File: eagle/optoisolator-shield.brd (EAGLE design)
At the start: 101.6 x 53.3 mm, 51 parts, among them Q1 NPN, Q2 NPN, Q3 NPN, Q4 NPN, Q5 NPN, Q6 NPN, U1 OPTO, U2 OPTO, U3 OPTO

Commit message: fixed XIO orientation error propagated from HackEEG shield
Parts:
- moved U$5 4.46 mm to (1.78, 5.89)
- moved U$2 0.05 mm to (1.78, 51.9)
- turned JP4 to 270 degrees
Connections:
- removed net N$602: JP4.35, JP4.36
- net GND: now also JP4.35, JP4.36
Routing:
- net D41: track 99.1 -> 126.9 mm, vias 3 -> 2
- net D43: track 84.5 -> 105.5 mm, vias 1 -> 0
- net D42: track 89.7 -> 105.8 mm
- net D40: track 91.5 -> 84.1 mm
- net D38: track 104.9 -> 98.5 mm
- net D45: track 90.8 -> 94.6 mm
- net D39: track 92.3 -> 96.0 mm
- net D44: track 94.9 -> 91.8 mm
- net N$602: track 2.54 -> 0.00 mm
- net OPTO_OUT_1B: track 76.1 -> 77.3 mm
- removed copper zone on layer 1, net D43
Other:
- board text added: "0"
- board text added: "1"
- board text added: "10"
- board text added: "11"
- board text added: "12"
- board text added: "13"
- board text added: "14"
- board text added: "15"
- board text added: "16"
- board text added: "17"
- board text added: "18"
- board text added: "19"
- board text added: "2"
- board text added: "20"
- board text added: "21"
- board text added: "22"
- board text added: "23"
- board text added: "24"
- board text added: "25"
- board text added: "26"
- board text added: "27"
- board text added: "28"
- board text added: "29"
- board text added: "3"
- board text added: "30"
- board text added: "31"
- board text added: "32"
- board text added: "33"
- board text added: "34"
- board text added: "35"
- board text added: "36"
- board text added: "37"
- board text added: "38"
- board text added: "3V3"
- board text added: "4"
- board text added: "46"
- board text added: "47"
- board text added: "48"
- board text added: "49"
- board text added: "5"
- board text added: "50"
- board text added: "51"
- board text added: "52"
- board text added: "53"
- board text added: "5V"
- board text added: "6"
- board text added: "7"
- board text added: "8"
- board text added: "9"
- board text added: "A0"
- board text added: "A1"
- board text added: "A10"
- board text added: "A11"
- board text added: "A12"
- board text added: "A13"
- board text added: "A14"
- board text added: "A15"
- board text added: "A2"
- board text added: "A3"
- board text added: "A4"
- board text added: "A5"
- board text added: "A6"
- board text added: "A7"
- board text added: "A8"
- board text added: "A9"
- board text added: "AREF"
- board text added: "GND"
- board text added: "IOREF"
- board text added: "RESET"
- board text added: "SCL1"
- board text added: "SDA1"
- board text added: "StarCat Optoisolator Shield"
- board text added: "VIN"
- board text added: "v1.1"
- board text removed: "StarCat Optoisolator Shield v1.0"

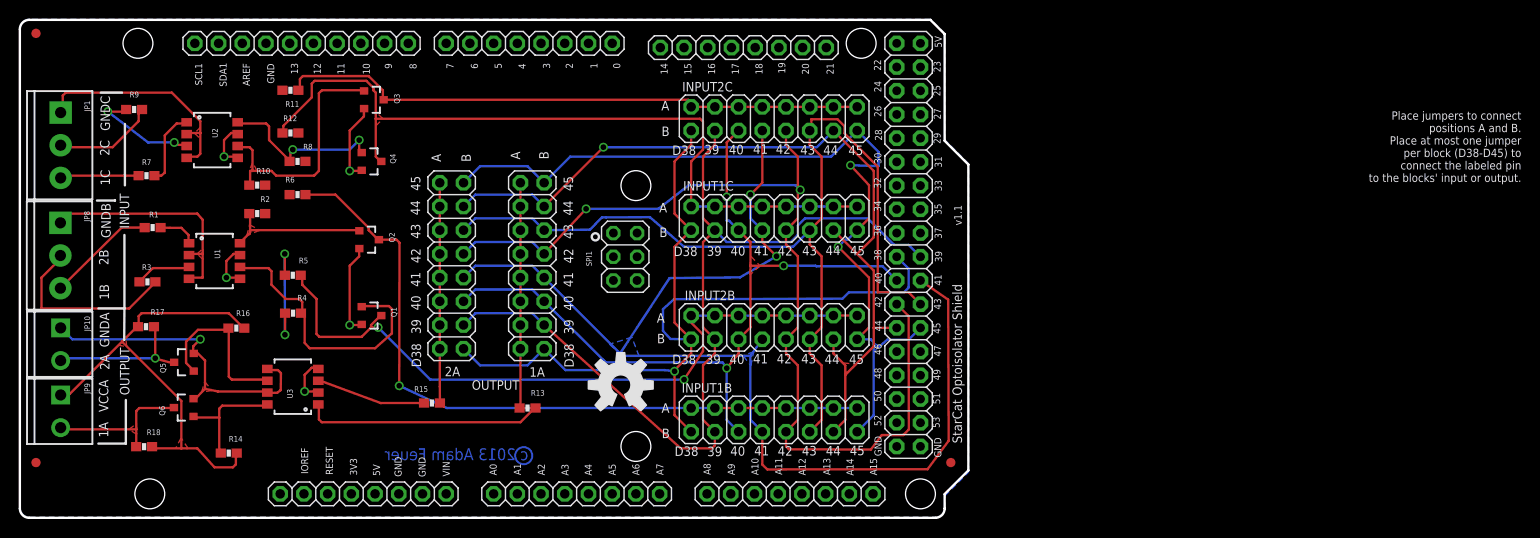
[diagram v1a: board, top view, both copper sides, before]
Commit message: updated silkscreen with correct dac0/1 and canrx/tx labels; updated fiducials so 2 share the same X and 2 share the same Y coordinates
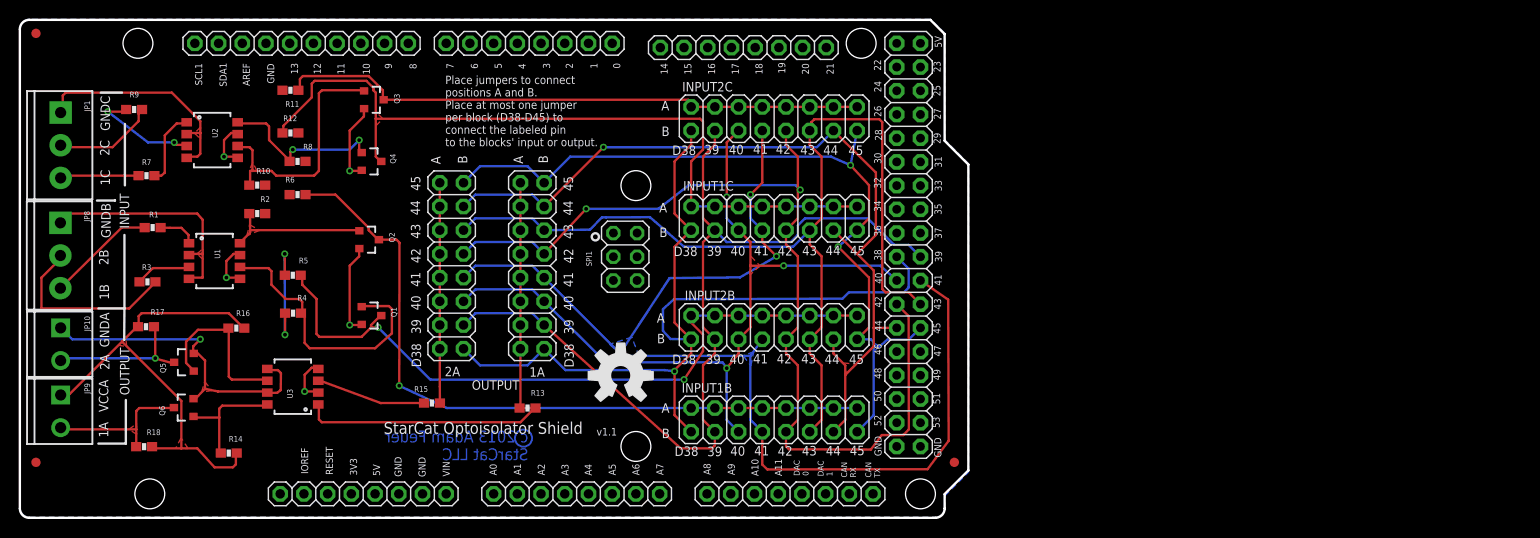
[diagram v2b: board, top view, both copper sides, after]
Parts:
- Q1, Q2, Q3, Q4, Q5, Q6: value NPN -> MMBT2222ALT3G
- moved U$1 1.02 mm to (64.4, 15.2)
- moved U$6 0.38 mm to (100.2, 5.92)
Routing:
- net D45: track 94.6 -> 88.9 mm
- net D43: track 105.5 -> 107.5 mm
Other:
- board text added: "CAN RX"
- board text added: "CAN TX"
- board text added: "DAC 0"
- board text added: "DAC 1"
- board text added: "c 2013 Adam Feuer StarCat LLC"
- board text removed: "A12"
- board text removed: "A13"
- board text removed: "A14"
- board text removed: "A15"
- board text removed: "c 2013 Adam Feuer"

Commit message: improved trace clearances; changed names of inputs from 1A... to A1... for better readability
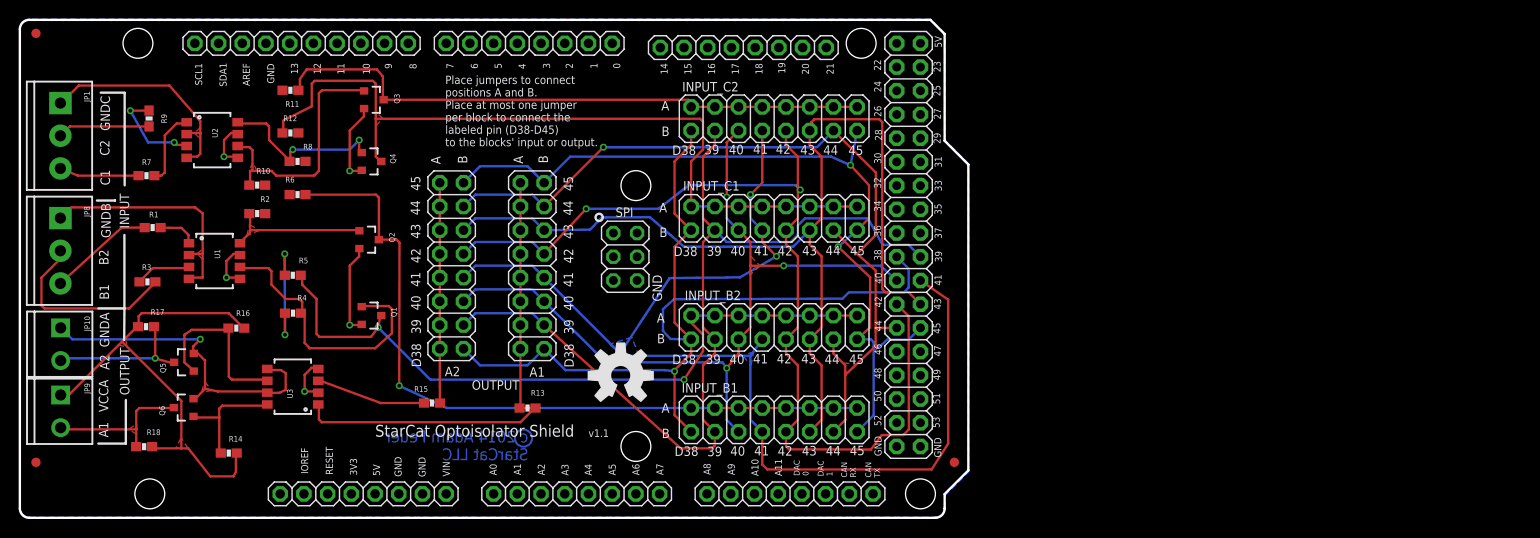
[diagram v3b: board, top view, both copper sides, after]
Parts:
- moved R9 1.87 mm to (13.9, 42.7), turned to 270 degrees
- moved JP1 1.02 mm to (4.39, 44.4)
- moved JP8 0.51 mm to (4.39, 32.1)
- renumbered 1A to A1, 2A to A2, INPUT1B to INPUT_B1, INPUT1C to INPUT_C1, INPUT2B to INPUT_B2, INPUT2C to INPUT_C2, SPI1 to SPI
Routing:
- net OPTO_OUT_1B: track 77.3 -> 79.8 mm
- net N$23: track 12.0 -> 10.2 mm
- net OPTO_OUT_2C: track 63.4 -> 65.0 mm
- net EXT_VCC: track 50.0 -> 51.5 mm
- net IN4: track 11.0 -> 9.91 mm
- net OPTO_OUT_1C: track 84.5 -> 85.5 mm
- net EXT_GND_2: track 35.5 -> 36.5 mm
- net OUT2N3: track 18.2 -> 18.8 mm
- net EXT_GND_1: track 24.7 -> 24.1 mm
- net D39: track 96.0 -> 96.5 mm
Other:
- board text added: "B1"
- board text added: "B2"
- board text added: "C1"
- board text added: "C2"
- board text added: "Place jumpers to connect positions A and B. Place at most one jumper per block to connect the labeled pin (D38-D45) to the blocks' input or output."
- board text added: "c 2014 Adam Feuer StarCat LLC"
- board text removed: "1A"
- board text removed: "1B"
- board text removed: "1C"
- board text removed: "2A"
- board text removed: "2B"
- board text removed: "2C"
- board text removed: "Place jumpers to connect positions A and B. Place at most one jumper per block (D38-D45) to connect the labeled pin to the blocks' input or output."
- board text removed: "c 2013 Adam Feuer StarCat LLC"

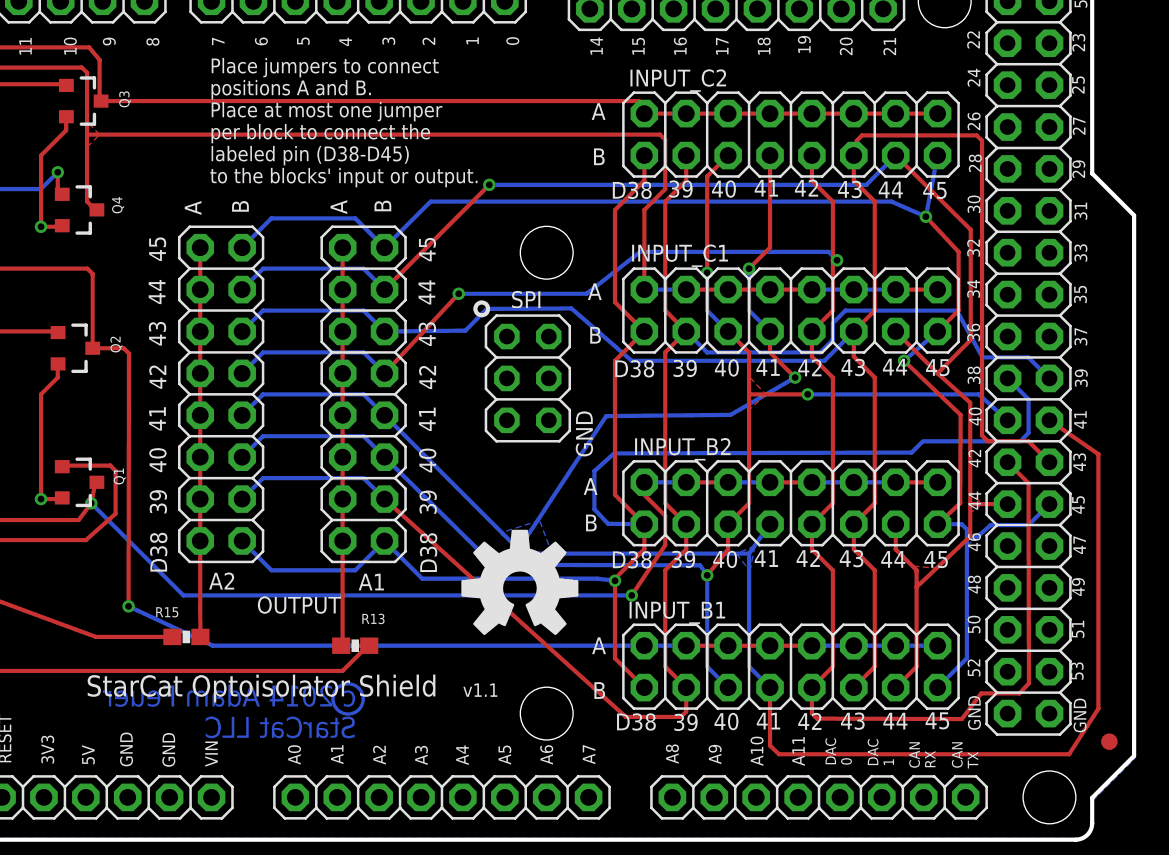
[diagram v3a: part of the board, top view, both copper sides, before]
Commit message: updated schematic renaming inputs/outputs 1A... to A1... for clarity
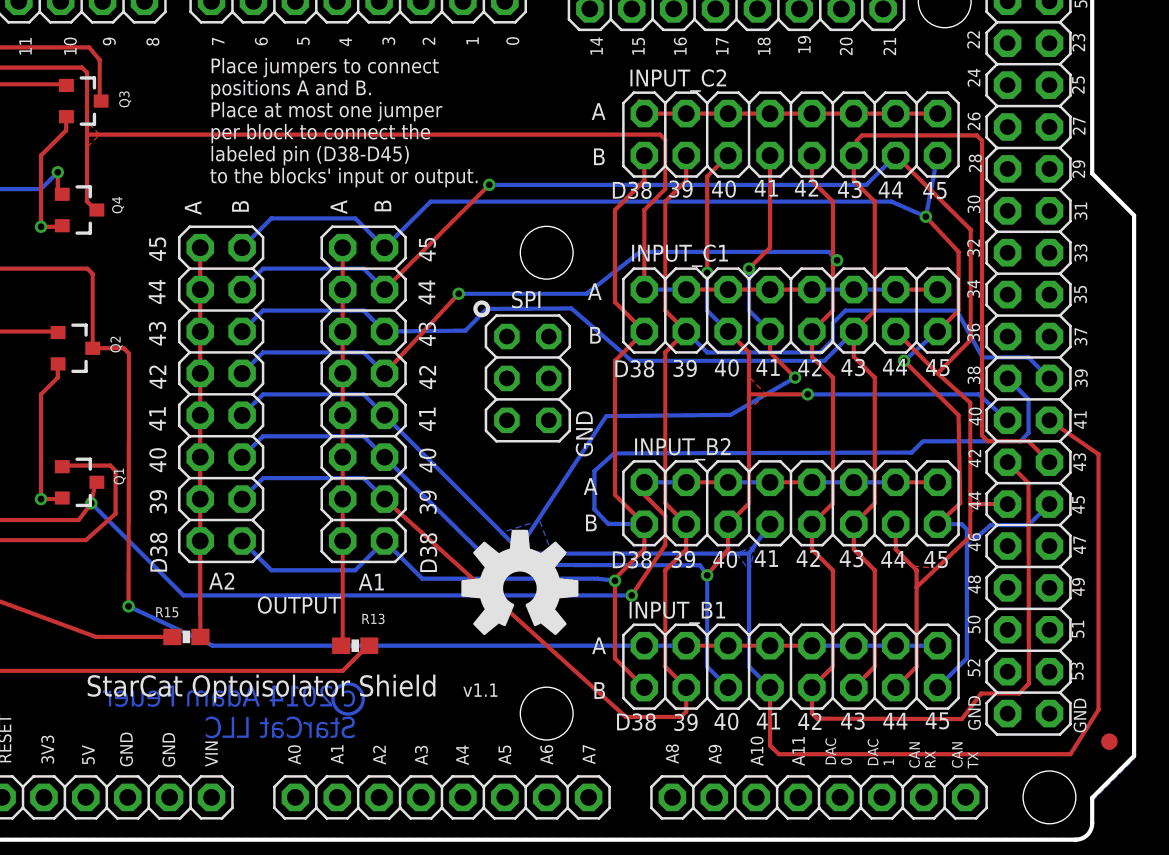
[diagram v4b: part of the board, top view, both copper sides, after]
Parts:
- U1, U2, U3: value OPTO -> ILD213T
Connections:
- net IN1 renamed IN_B1
- net IN2 renamed IN_B2
- net IN3 renamed IN_C1
- net IN4 renamed IN_C2
- net OPTO_IN_1A renamed OPTO_IN_A1
- net OPTO_IN_2A renamed OPTO_IN_A2
- net OPTO_OUT_1B renamed OPTO_OUT_B1
- net OPTO_OUT_1C renamed OPTO_OUT_C1
- net OPTO_OUT_2B renamed OPTO_OUT_B2
- net OUT5 renamed OUT_A1
- net OUT6 renamed OUT_A2
- new net OPTO_OUT_C2: Q3.3, R11.1
- net OPTO_OUT_2C: no longer Q3.3, R11.1
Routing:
- net OPTO_OUT_2C: track 65.0 -> 18.7 mm
- net OPTO_OUT_C2: track 0.00 -> 13.7 mm
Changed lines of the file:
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@@
 <element name="U$6" library="adafruit" package="FIDUCIAL_1MM" value="FIDUCIAL" x="100.1522" y="5.9182" smashed="yes"/>
 <element name="U$2" library="adafruit" package="FIDUCIAL_1MM" value="FIDUCIAL" x="1.778" y="51.8668" smashed="yes"/>
-<element name="U2" library="SparkFun" package="SO08-2" value="OPTO" x="20.6502" y="40.4368" smashed="yes" rot="R270">
+<element name="U2" library="SparkFun" package="SO08-2" value="ILD213T" x="20.6502" y="40.4368" smashed="yes" rot="R270">
 <attribute name="VALUE" x="20.0152" y="41.7068" size="0.4064" layer="27" rot="R270"/>
 <attribute name="NAME" x="20.6502" y="41.7068" size="0.6096" layer="25" font="vector" rot="R270"/>
@@
 <attribute name="VALUE" x="5.6642" y="45.6692" size="0.4064" layer="27" rot="R270"/>
 </element>
-<element name="U1" library="SparkFun" package="SO08-2" value="OPTO" x="20.9042" y="27.4828" smashed="yes" rot="R270">
+<element name="U1" library="SparkFun" package="SO08-2" value="ILD213T" x="20.9042" y="27.4828" smashed="yes" rot="R270">
 <attribute name="VALUE" x="20.2692" y="28.7528" size="0.4064" layer="27" rot="R270"/>
 <attribute name="NAME" x="20.9042" y="28.7528" size="0.6096" layer="25" font="vector" rot="R270"/>
@@
 <attribute name="VALUE" x="5.6642" y="33.3502" size="0.4064" layer="27" rot="R270"/>
 </element>
-<element name="U3" library="SparkFun" package="SO08-2" value="OPTO" x="29.2862" y="14.0208" smashed="yes" rot="R90">
+<element name="U3" library="SparkFun" package="SO08-2" value="ILD213T" x="29.2862" y="14.0208" smashed="yes" rot="R90">
 <attribute name="VALUE" x="29.9212" y="12.7508" size="0.4064" layer="27" rot="R90"/>
 <attribute name="NAME" x="29.2862" y="12.7508" size="0.6096" layer="25" font="vector" rot="R90"/>
@@
 <wire x1="28.448" y1="19.5834" x2="28.4616" y2="21.8948" width="0.254" layer="1"/>
 </signal>
-<signal name="IN2">
+<signal name="IN_B2">
 <contactref element="R3" pad="2"/>
 <contactref element="JP8" pad="2"/>
@@
 <wire x1="14.5542" y1="25.1968" x2="14.566" y2="25.2476" width="0.254" layer="1"/>
 </signal>
-<signal name="IN1">
+<signal name="IN_B1">
 <contactref element="R1" pad="1"/>
 <contactref element="JP8" pad="3"/>
@@
 <contactref element="JP4" pad="14"/>
 </signal>
-<signal name="IN3">
+<signal name="IN_C1">
 <contactref element="R7" pad="1"/>
 <contactref element="JP1" pad="3"/>
@@
 <wire x1="6.2738" y1="36.6268" x2="4.3942" y2="37.3992" width="0.254" layer="1"/>
 </signal>
-<signal name="IN4">
+<signal name="IN_C2">
 <contactref element="R9" pad="2"/>
 <contactref element="JP1" pad="2"/>
@@
 <wire x1="59.0042" y1="38.6588" x2="56.2102" y2="35.8648" width="0.254" layer="16"/>
 <wire x1="91.1098" y1="20.3708" x2="89.7382" y2="19.1008" width="0.254" layer="1"/>
-<wire x1="91.1352" y1="25.7302" x2="91.1098" y2="20.3708" width="0.254" layer="1"/>
-<wire x1="87.7062" y1="29.0068" x2="91.1352" y2="25.7302" width="0.254" layer="1"/>
+<wire x1="91.0082" y1="25.7048" x2="91.1098" y2="20.3708" width="0.254" layer="1"/>
+<wire x1="87.7062" y1="29.0068" x2="91.0082" y2="25.7048" width="0.254" layer="1"/>
 <via x="89.027" y="37.7444" extent="1-16" drill="0.4064"/>
 <via x="87.7062" y="29.0068" extent="1-16" drill="0.4064"/>
@@
 </polygon>
 <wire x1="99.4918" y1="23.3426" x2="96.52" y2="25.4" width="0.254" layer="1"/>
-<wire x1="99.4918" y1="7.9248" x2="99.4918" y2="23.3426" width="0.254" layer="1"/>
-<wire x1="97.7138" y1="5.1562" x2="99.4918" y2="7.9248" width="0.254" layer="1"/>
+<wire x1="99.4918" y1="7.8486" x2="99.4918" y2="23.3426" width="0.254" layer="1"/>
+<wire x1="97.79" y1="5.1562" x2="99.4918" y2="7.8486" width="0.254" layer="1"/>
 <wire x1="79.5782" y1="5.6769" x2="80.1243" y2="5.1562" width="0.254" layer="1"/>
-<wire x1="80.1243" y1="5.1562" x2="97.7138" y2="5.1562" width="0.254" layer="1"/>
+<wire x1="80.1243" y1="5.1562" x2="97.79" y2="5.1562" width="0.254" layer="1"/>
 <wire x1="79.5782" y1="5.6769" x2="79.5782" y2="9.1948" width="0.254" layer="1"/>
 </signal>
@@
 <wire x1="26.4922" y1="11.9888" x2="26.5557" y2="12.1158" width="0.254" layer="1"/>
 </signal>
-<signal name="OUT5">
+<signal name="OUT_A1">
 <contactref element="Q6" pad="3"/>
 <contactref element="R18" pad="1"/>
@@
 </polygon>
 </signal>
-<signal name="OUT6">
+<signal name="OUT_A2">
 <contactref element="Q5" pad="3"/>
 <contactref element="R17" pad="1"/>
@@
 </polygon>
 </signal>
-<signal name="OPTO_OUT_1B">
+<signal name="OPTO_OUT_B1">
 <contactref element="Q2" pad="3"/>
 <contactref element="R6" pad="1"/>
@@
 <wire x1="38.5142" y1="34.2773" x2="38.5142" y2="29.7688" width="0.254" layer="1"/>
 </signal>
-<signal name="OPTO_OUT_2B">
+<signal name="OPTO_OUT_B2">
 <contactref element="Q1" pad="3"/>
 <contactref element="R5" pad="1"/>
@@
 <wire x1="37.6682" y1="19.3548" x2="38.4302" y2="20.3708" width="0.254" layer="1"/>
 </signal>
-<signal name="OPTO_OUT_1C">
+<signal name="OPTO_OUT_C1">
 <contactref element="Q4" pad="3"/>
 <contactref element="R12" pad="1"/>
@@
 </signal>
 <signal name="OPTO_OUT_2C">
-<contactref element="Q3" pad="3"/>
-<contactref element="R11" pad="1"/>
 <contactref element="INPUT_C2" pad="2"/>
 <contactref element="INPUT_C2" pad="4"/>
@@
 <contactref element="INPUT_C2" pad="14"/>
 <contactref element="INPUT_C2" pad="16"/>
-<wire x1="38.9382" y1="47.244" x2="38.9382" y2="44.7548" width="0.254" layer="1"/>
-<wire x1="38.3032" y1="48.006" x2="38.9382" y2="47.244" width="0.254" layer="1"/>
-<wire x1="30.0482" y1="45.7708" x2="30.0482" y2="46.9773" width="0.254" layer="1"/>
-<wire x1="30.0482" y1="46.9773" x2="30.7721" y2="48.006" width="0.254" layer="1"/>
-<wire x1="30.7721" y1="48.006" x2="38.3032" y2="48.006" width="0.254" layer="1"/>
-<wire x1="38.9382" y1="44.7548" x2="39.0222" y2="44.7548" width="0.254" layer="1"/>
-<wire x1="30.0482" y1="45.7708" x2="29.8822" y2="45.7708" width="0.254" layer="1"/>
 <wire x1="74.4982" y1="43.9928" x2="71.9582" y2="43.9928" width="0.254" layer="1"/>
 <wire x1="74.4982" y1="43.9928" x2="77.0382" y2="43.9928" width="0.254" layer="1"/>
@@
 <wire x1="71.9582" y1="43.9928" x2="71.9582" y2="44.4373" width="0.254" layer="1"/>
 <wire x1="71.9582" y1="44.4373" x2="71.6407" y2="44.7548" width="0.254" layer="1"/>
-<wire x1="71.6407" y1="44.7548" x2="39.0222" y2="44.7548" width="0.254" layer="1"/>
-</signal>
-<signal name="OPTO_IN_1A">
+</signal>
+<signal name="OPTO_IN_A1">
 <contactref element="R13" pad="1"/>
 <contactref element="A1" pad="2"/>
@@
 <wire x1="53.6702" y1="28.2448" x2="53.6702" y2="30.7848" width="0.254" layer="1"/>
 </signal>
-<signal name="OPTO_IN_2A">
+<signal name="OPTO_IN_A2">
 <contactref element="R15" pad="2"/>
 <contactref element="A2" pad="2"/>
@@
 <contactref element="SPI" pad="6"/>
 </signal>
+<signal name="OPTO_OUT_C2">
+<contactref element="Q3" pad="3"/>
+<contactref element="R11" pad="1"/>
+<wire x1="38.9382" y1="47.244" x2="38.9382" y2="44.7548" width="0.254" layer="1"/>
+<wire x1="38.3032" y1="48.006" x2="38.9382" y2="47.244" width="0.254" layer="1"/>
+<wire x1="30.0482" y1="45.7708" x2="30.0482" y2="46.9773" width="0.254" layer="1"/>
+<wire x1="30.0482" y1="46.9773" x2="30.7721" y2="48.006" width="0.254" layer="1"/>
+<wire x1="30.7721" y1="48.006" x2="38.3032" y2="48.006" width="0.254" layer="1"/>
+<wire x1="38.9382" y1="44.7548" x2="39.0222" y2="44.7548" width="0.254" layer="1"/>
+<wire x1="30.0482" y1="45.7708" x2="29.8822" y2="45.7708" width="0.254" layer="1"/>
+</signal>
 </signals>
